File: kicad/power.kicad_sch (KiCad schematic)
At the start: 117 parts, among them J1 12 V in (5.5x2.1), J2 TX power (shunt), U1 TPS54302DDCR, U2 TPS65131RGER, U3 TPS7A4700RGWT, U4 TPS7A3301RGWR, U5 LM2731XMF, U6 TLV75733PDBVR, U7 TPS7A4700RGWT, U8 TPS26600PWPR

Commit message: Board ready for routing: power sheets redrawn, 3D models, test access, routing setup
Schematic
- Power supply split into two boxed A3 sheets (Power 1: input, +5V, VDRV,
  +3V3, 3V3_MIC; Power 2: analog +-6V5, +-5VA, +3V3A and the bring-up notes);
  eFuse wired inline; text no longer clashes; ferrite drawn as L_Ferrite.
- Every page of the schematic PDF is A3 (cells scaled up, array redrawn).
- RX_OUT test pad on every channel; four more GND test points.
- Test pads and solder jumpers out of the BOM, like their footprints.

Board
- 3D model for every part (make_3d.py for the CUSP-TR80, stock substitutes
  for four missing library models); check_design checks it.
- JLC04161H-7628 stackup, ENIG; inner GND layers typed as planes; thermal
  reliefs on through-hole pads; HighCurrent net class (1 mm).
- Custom DRC rules (aesa.kicad_dru): TX/RX and switch-node separation,
  clock spacing, JLCPCB limits.
- Footprints keep their library IDs (schematic parity clean); assembly
  drawing docs/assembly/aesa_assembly.pdf.
- Freerouting 2.5.0 installed; DSN export checked.

ERC 0, DRC 0, design check 19/19, placement checks 12/12.
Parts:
- removed C11, C12, C24, C25, C40, C41: 10u 16V X7R 1206, Capacitor_SMD:C_1206_3216Metric, symbol Device:C
- removed C13: 100n 16V X7R, Capacitor_SMD:C_0603_1608Metric, symbol Device:C
- removed C14: 6.8p 50V C0G, Capacitor_SMD:C_0603_1608Metric, symbol Device:C
- removed C15, C16, C21, C22, C23, C27, C39: 10u 25V X7R 1206, Capacitor_SMD:C_1206_3216Metric, symbol Device:C
- removed C17: 7.5p 50V C0G, Capacitor_SMD:C_0603_1608Metric, symbol Device:C
- removed C18: 220n 16V X7R, Capacitor_SMD:C_0603_1608Metric, symbol Device:C
- removed C19: 10n 16V X7R, Capacitor_SMD:C_0603_1608Metric, symbol Device:C
- removed C20: 4.7n 50V C0G, Capacitor_SMD:C_0603_1608Metric, symbol Device:C
- removed C26, C28, C42: 1u 16V X7R, Capacitor_SMD:C_0603_1608Metric, symbol Device:C
- removed C29: 10n 50V C0G, Capacitor_SMD:C_0603_1608Metric, symbol Device:C
- removed C30: 22u 16V X7R 1210, Capacitor_SMD:C_1210_3225Metric, symbol Device:C
- removed D4, D6: SS14, Diode_SMD:D_SMA, symbol Device:D_Schottky
- removed D5, D7: green, LED_SMD:LED_0603_1608Metric, symbol Device:LED
- removed FB1: 600R@100MHz 0603, Inductor_SMD:L_0603_1608Metric, symbol Device:FerriteBead
- removed JP2, JP3, JP5, JP6, JP7: cut to isolate, Jumper:SolderJumper-2_P1.3mm_Bridged_RoundedPad1.0x1.5mm, symbol Jumper:SolderJumper_2_Bridged
- removed L2, L3: 4.7u Isat>=2A, Inductor_SMD:L_Sunlord_SWPA6045S, symbol Device:L
- removed R10, R13: 3.3k 1%, Resistor_SMD:R_0603_1608Metric, symbol Device:R
- removed R11: 649k 1%, Resistor_SMD:R_0603_1608Metric, symbol Device:R
- removed R12: 121k 1%, Resistor_SMD:R_0603_1608Metric, symbol Device:R
- removed R14: 715k 1%, Resistor_SMD:R_0603_1608Metric, symbol Device:R
- removed R15: 220k 1%, Resistor_SMD:R_0603_1608Metric, symbol Device:R
- removed R7: 100 1%, Resistor_SMD:R_0603_1608Metric, symbol Device:R
- removed R8: 562k 1%, Resistor_SMD:R_0603_1608Metric, symbol Device:R
- removed R9: 130k 1%, Resistor_SMD:R_0603_1608Metric, symbol Device:R
- removed TP12: TP +3V3A, TestPoint:TestPoint_Pad_D1.5mm, symbol Connector:TestPoint
- removed TP3: TP +6V5, TestPoint:TestPoint_Pad_D1.5mm, symbol Connector:TestPoint
- removed TP4: TP -6V5, TestPoint:TestPoint_Pad_D1.5mm, symbol Connector:TestPoint
- removed TP5: TP +5VA, TestPoint:TestPoint_Pad_D1.5mm, symbol Connector:TestPoint
- removed TP6: TP -5VA, TestPoint:TestPoint_Pad_D1.5mm, symbol Connector:TestPoint
- removed U2: TPS65131RGER, Package_DFN_QFN:VQFN-24-1EP_4x4mm_P0.5mm_EP2.45x2.45mm_ThermalVias, symbol Regulator_Switching:TPS65130RGE
- removed U3, U7: TPS7A4700RGWT, Package_DFN_QFN:Texas_RGW0020A_VQFN-20-1EP_5x5mm_P0.65mm_EP3.15x3.15mm_ThermalVias, symbol Regulator_Linear:TPS7A4701xRGW
- removed U4: TPS7A3301RGWR, Package_DFN_QFN:Texas_RGW0020A_VQFN-20-1EP_5x5mm_P0.65mm_EP3.15x3.15mm_ThermalVias, symbol Regulator_Linear:TPS7A3301RGW
- added FB1: 600R@100MHz 0603, Inductor_SMD:L_0603_1608Metric, symbol Device:L_Ferrite
- added TP16, TP17, TP18, TP19: GND, TestPoint:TestPoint_Pad_D1.5mm, symbol Connector:TestPoint
- JP1, JP4: now left out of the parts list
- TP1: value TP VIN -> VIN; now left out of the parts list
- TP10, TP9: value TP GND -> GND; now left out of the parts list
- TP11: value TP 3V3_MIC -> 3V3_MIC; now left out of the parts list
- TP13: value TP VIN_JACK -> VIN_JACK; now left out of the parts list
- TP14: value TP IMON -> IMON; now left out of the parts list
- TP15: value TP FLT -> FLT; now left out of the parts list
- TP2: value TP +5V -> +5V; now left out of the parts list
- TP7: value TP VDRV -> VDRV; now left out of the parts list
- TP8: value TP +3V3 -> +3V3; now left out of the parts list
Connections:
- net +3V3: now also FB1.1
- net 3V3_MIC: now also FB1.2
- net GND: now also TP16.1, TP17.1, TP18.1, TP19.1
- net EF_DVDT: no longer names the net of C43.1, U8.12 (dVdT)
- net EF_FLT: no longer names the net of R27.2, TP15.1, U8.14 (~{FLT})
- net EF_ILIM: no longer names the net of R25.1, U8.11 (ILIM)
- net EF_IMON: no longer names the net of R26.1, TP14.1, U8.10 (IMON)
- net EF_OVP: no longer names the net of R23.2, R24.1, U8.5 (OVP)
- net EF_UVLO: no longer names the net of R22.2, R23.1, U8.3 (UVLO)
- net LED_+3V3: no longer names the net of D10.2 (A), R20.2
- net LED_+5V: no longer names the net of D3.2 (A), R6.2
- net LED_3V3_MIC: no longer names the net of D11.2 (A), R21.2
- net LED_VDRV: no longer names the net of D9.2 (A), R19.2
- net LED_VIN: no longer names the net of D2.2 (A), R1.2
- no-connect marks 19 -> 3
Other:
- note added: "1 A, stable with ceramic caps. Load < 0.15 A: ADC IOVDD, clock buffers, logic, mics."
- note added: "1.23 V x (1 + 150k/13k) = 15.4 V. Load, all 64 elements in CW at 40 kHz: about 0.24 A (sim/reports/tx_cw.md). Remove the"
- note added: "1.6 A. F1 (2 A polyfuse) backs it up."
- note added: "A. 12 V INPUT: jack -> TPS26600 eFuse -> polyfuse -> VIN"
- note added: "E. VDRV 15 V: LM2731X boost from VIN"
- note added: "F. +3V3: TLV75733P LDO from +5V"
- note added: "Ferrite-filtered +3V3 for the 8 MEMS mics. Remove FB1 to isolate."
- note added: "G. GROUND"
- note added: "H. 3V3_MIC: mic supply"
- note added: "J2 shunt to unpower every TX driver."
- note added: "One GND net and plane (In1, In2). Scope-ground test points: TP9/TP10 at the"
- note added: "Power tree and bring-up checklist: Power 2."
- note added: "UVLO/OVP divider 100k / 5.6k / 10k. ILIM 12 k/A -> 7.5k = 1.6 A. dVdT 22 nF: 5 V/ms soft start. IMON 72 uA/A into 15k = 1.08 V/A (TP IMON). FLT"
- note added: "Vout = 0.596 V x (1 + 75k/10k) = 5.07 V. EN UVLO about 7.3 V. Load about 1.6 A. SW_5V loop (C3, U1, L1) kept tight on the board."
- note added: "eFuse U8 (resettable, auto-retry): rated +-60 V (reverse polarity), on above 8.8 V, off above 13.8 V (protects the 14.5 V LM2731), current limit"
- note added: "low = fault (TP FLT). MODE open = auto-retry, SHDN open = on."
- note added: "power supply, TP16-TP19 spread over the board (ADC row, array sides, TX row)."
- note removed: "+5VA: ANY-OUT 1.4 + 3.2 + 0.4 = 5.0 V. -5VA = -1.176 V x (1 + 715k/220k) = -5.00 V."
- note removed: "+6V5 = 1.213 V x (1 + 562k/130k) = 6.46 V. -6V5 = -1.213 V x 649k/121k = -6.51 V."
- note removed: "1.23 V x (1 + 150k/13k) = 15.4 V. Load, all 64 elements in CW at 40 kHz: about 0.24 A (sim/reports/tx_cw.md)."
- note removed: "A. 12 V INPUT: jack -> TPS26600 eFuse (resettable: auto-retry) -> polyfuse (back-up) -> VIN"
- note removed: "ANY-OUT 1.4 + 1.6 + 0.2 + 0.1 = 3.3 V. Load about 0.45 A (16 x TLV320ADC5140); 0.8 W in the LDO, thermal vias under the pad."
- note removed: "C. +-6V5: TPS65131RGER boost + inverter from +5V (feeds the analog LDOs only)"
- note removed: "D. ANALOG RAILS: TPS7A4700 +5VA, TPS7A3301 -5VA (low noise, no LEDs)"
- note removed: "Drawn with the pin-identical TPS65130 symbol: order TPS65131RGER (2 A switches). PSP/PSN low: fixed-frequency PWM."
- note removed: "E. VDRV 15 V: LM2731X boost from VIN. Remove the J2 shunt to unpower all TX drivers"
- note removed: "F. +3V3: TLV75733P LDO from +5V (1 A, stable with ceramic caps)"
- note removed: "G. GROUND: one GND net and plane"
- note removed: "H. 3V3_MIC: ferrite-filtered supply for the 8 MEMS mics (remove FB1 to isolate)"
- note removed: "I. +3V3A: TPS7A4700 low-noise LDO from +5V for the 16 ADCs' AVDD (analog rail: no LED)"
- note removed: "Load < 0.15 A: ADC IOVDD, clock buffers, logic, mics."
- note removed: "Load: 64 x OPA1678 (4 mA per channel): about 0.3 A on +5VA and on -5VA."
- note removed: "Test points for scope grounds."
- note removed: "UVLO/OVP divider 100k / 5.6k / 10k: on 8.8 V, off 13.8 V. ILIM 12 k/A -> 7.5 k = 1.6 A. dVdT 22 nF: 5 V/ms. IMON 72 uA/A into 15 k = 1.08 V/A (TP14). FLT low = fault (TP15)."
- note removed: "Vout = 0.596 V x (1 + 75k/10k) = 5.07 V. EN UVLO about 7.3 V. Load about 1.6 A."
- note removed: "eFuse: input rated 60 V and -60 V (reverse polarity), switches off above 13.8 V (protects the 14.5 V LM2731) and below 8.8 V, current limit 1.6 A."
- title: Power: 12 V in, +5V, +-6V5, +-5VA, VDRV, +3V3, 3V3_MIC, +3V3A -> Power 1: 12 V input, +5V, VDRV (TX), +3V3, 3V3_MIC

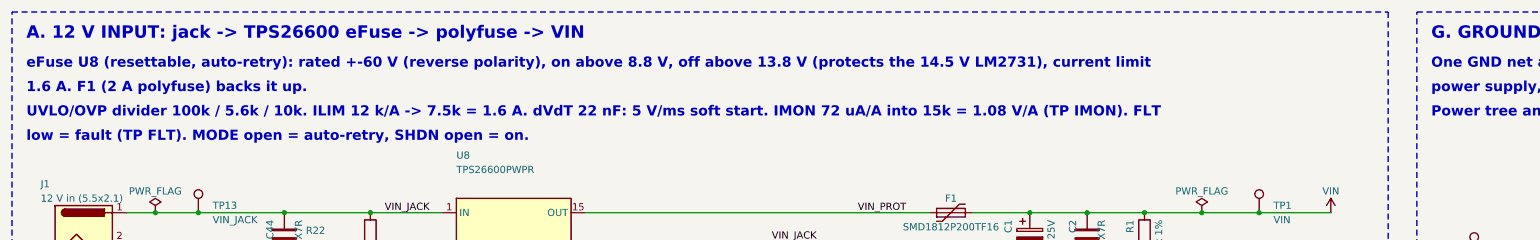
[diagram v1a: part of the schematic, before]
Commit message: Fix small inconsistencies: one revision (rev 1, 2026-10-24) for sheets and board
- REV/DATE come from scripts/common.py for every title block and the board
  silkscreen (the sheets said rev 2, the board rev 1).
- Channel note: +27 dB is element -> amplifier output; the ADC pin sees
  +16.5 dB after the divider.
- Board input text 8.8-13.8 V (eFuse UVLO); LM2731 limit 14 V (14.5 V abs max).
- Brief/README: real board size 192 x 301 mm, CUSP-TR80 footprint and pitch
  note, nominal vs simulated gain, board test-point references, 126 pages.
- SKiDL spec uses L_Ferrite like the sheet; dead AD7606/net-tie entries gone.

ERC 0, DRC 0, design check 19/19, placement checks 12/12.
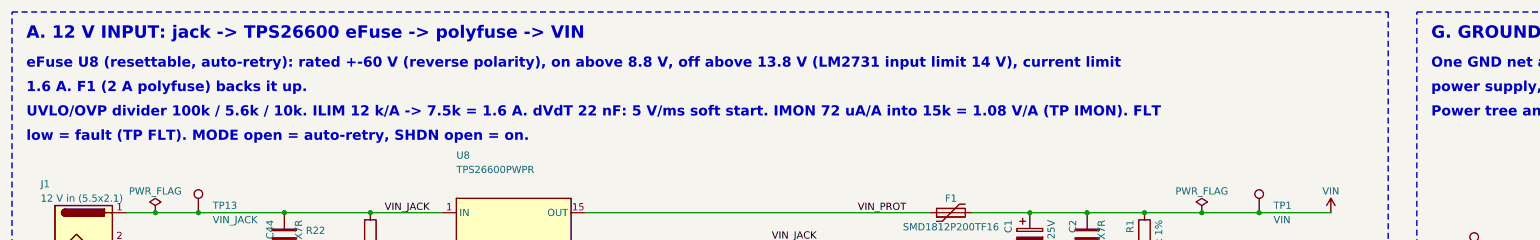
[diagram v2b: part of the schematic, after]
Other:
- note added: "eFuse U8 (resettable, auto-retry): rated +-60 V (reverse polarity), on above 8.8 V, off above 13.8 V (LM2731 input limit 14 V), current limit"
- note removed: "eFuse U8 (resettable, auto-retry): rated +-60 V (reverse polarity), on above 8.8 V, off above 13.8 V (protects the 14.5 V LM2731), current limit"
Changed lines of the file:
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@@
 	(title_block
 		(title "Power 1: 12 V input, +5V, VDRV (TX), +3V3, 3V3_MIC")
-		(date "2026-10-20")
-		(rev "2")
+		(date "2026-10-24")
+		(rev "1")
 		(company "Hybrid 8x8 ultrasonic AESA")
 	)
@@
 		)
 	)
-	(text "eFuse U8 (resettable, auto-retry): rated +-60 V (reverse polarity), on above 8.8 V, off above 13.8 V (protects the 14.5 V LM2731), current limit"
+	(text "eFuse U8 (resettable, auto-retry): rated +-60 V (reverse polarity), on above 8.8 V, off above 13.8 V (LM2731 input limit 14 V), current limit"
 		(exclude_from_sim no)
 		(at 20.32 30.48 0)

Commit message: Block-first routing: all repeated blocks routed and passing, power input and +-6V5 hand-routed
Schematic
- TX groups and ADC inputs numbered in order (TXG01 = DRV1-4, ADC IN1..4 = RX1..4).
- Power sheets renumbered 1-8 with real references; eFuse RTN no longer tied to GND (TPS2660 9.3.5.5).
- Damped 100 uF bulk caps at the far ends of VIN (C50) and +5V (C51); header clock RC filters removed;
  switch-node snubbers kept as DNP footprints.

Layout and routing
- New routing toolchain: route.py (block stages), block_routes.py (hand-made block routes), maze.py
  (45-degree grid router with rip-up and a per-net time budget), route_lib.py (bend45, chamfer, copper
  checks), block_check.py (DRC and internal nets per block instance), board/cell views.
- Channel, ADC, TX group, clock buffer, enable buffer, mic and header blocks routed and passing
  block_check; no right-angle corners left.
- Designed TX control bus; SDI taps keep 0.7 mm from clock copper.
- Power: 12 V input (eFuse, RTN island, FLT via the front copper) and TPS65131 +-6V5 section with fixed
  templates and hand routing; each power section counts as its own block; the +3V3 LED overflows into
  the gap beside its section.

docs/routing_and_emi.md describes the routing and EMI rules; sim/mic_clock_si adds the mic clock check.
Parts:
- added C45: 10u 50V X7R 1210, Capacitor_SMD:C_1210_3225Metric, symbol Device:C
- added C46, C49: 470p 50V C0G DNP, Capacitor_SMD:C_0603_1608Metric, symbol Device:C
- added C50, C51: 100u 25V, Capacitor_SMD:CP_Elec_8x10, symbol Device:C_Polarized
- added L5: 1u Isat>=4A, Inductor_SMD:L_Sunlord_SWPA4030S, symbol Device:L
- added R28, R31: 4.7 1% DNP, Resistor_SMD:R_0603_1608Metric, symbol Device:R
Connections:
- net +5V: now also C51.1
- net GND: now also C45.2, C46.2, C49.2, C50.2, C51.2; no longer C43.2, R24.2, R25.2, R26.2, U8.17 (RTN), U8.8 (RTN)
- net SW_5V: now also R28.1
- net SW_VDRV: now also R31.1
- net VIN: now also C50.1, L5.2; no longer F1.2
- new net: C49.1, R31.2
- new net: C46.1, R28.2
- new net EFUSE_RTN: C43.2, R24.2, R25.2, R26.2, U8.17 (RTN), U8.8 (RTN)
- new net VIN_F: C45.1, F1.2, L5.1
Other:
- note added: "(sim/reports/tx_cw.md). Remove the J9502 shunt to unpower every TX driver. R9531 + C9549: switch-node snubber, DNP (fit"
- note added: "/ TP9510 at the power supply, TP9516 - TP9519 spread over the board (ADC row,"
- note added: "1. 12 V INPUT: jack J9501 -> TPS26600 eFuse U9508 -> polyfuse F9501 -> VIN"
- note added: "1.23 V x (1 + 150k/13k) = 15.4 V (R9517 / R9518). Load, all 64 elements in CW at 40 kHz: about 0.24 A"
- note added: "1.6 A. Polyfuse F9501 (2 A) backs it up. C9545 - L9505 - C9501 keep the switchers' ripple off the cable."
- note added: "2. +5V: TPS54302 buck U9501 (TI reference design), 3 A"
- note added: "3. +3V3: TLV75733P LDO U9506 from +5V"
- note added: "4. VDRV 15 V: LM2731X boost U9505 from VIN"
- note added: "5. 3V3_MIC: mic supply"
- note added: "C9503 - U9501 - L9501 is kept tight on the board. R9528 + C9546: switch-node snubber, DNP (fit only if the switch node rings)."
- note added: "C9551 100 uF electrolytic: damped bulk at the end of the 300 mm +5V run from the buck,"
- note added: "Ferrite-filtered +3V3 for the 8 MEMS mics. Remove FB9501 to isolate."
- note added: "GROUND TEST POINTS"
- note added: "One GND net and plane (inner layers In1, In2). Scope-ground test points: TP9509"
- note added: "RTN (pin 8, PowerPad) and the support parts sit on EFUSE_RTN, apart from GND: the chip's reverse-polarity block is between RTN and GND (tying"
- note added: "UVLO/OVP divider R9522 / R9523 / R9524 (100k / 5.6k / 10k). ILIM R9525 7.5k = 1.6 A. dVdT C9543 22 nF: 5 V/ms soft start. IMON R9526 15k = 1.08"
- note added: "V/A (TP9514). FLT low = fault (TP9515). MODE open = auto-retry, SHDN open = on."
- note added: "Vout = 0.596 V x (1 + 75k/10k) = 5.07 V (R9504 / R9505). EN UVLO about 7.3 V (R9502 / R9503). Load about 1.6 A. The switching loop"
- note added: "both array sides, TX row). Power tree and bring-up checklist: Power 2."
- note added: "current local)."
- note added: "eFuse U9508 (resettable, auto-retry): rated +-60 V (reverse polarity), on above 8.8 V, off above 13.8 V (LM2731 input limit 14 V), current limit"
- note added: "for both top LDOs (U9506, U9507)."
- note added: "mm feed from the jack (its ESR damps the feed inductance against the ceramic input caps; keeps the switchers' ripple"
- note added: "only if the switch node rings). C9550 100 uF electrolytic: damped bulk on VIN at the power row, the far end of the 280"
- note added: "them disables it). Board: an RTN copper island under U9508, clear of the GND planes."
- note removed: "1.23 V x (1 + 150k/13k) = 15.4 V. Load, all 64 elements in CW at 40 kHz: about 0.24 A (sim/reports/tx_cw.md). Remove the"
- note removed: "1.6 A. F1 (2 A polyfuse) backs it up."
- note removed: "A. 12 V INPUT: jack -> TPS26600 eFuse -> polyfuse -> VIN"
- note removed: "B. +5V: TPS54302 buck (TI reference design), 3 A"
- note removed: "E. VDRV 15 V: LM2731X boost from VIN"
- note removed: "F. +3V3: TLV75733P LDO from +5V"
- note removed: "Ferrite-filtered +3V3 for the 8 MEMS mics. Remove FB1 to isolate."
- note removed: "G. GROUND"
- note removed: "H. 3V3_MIC: mic supply"
- note removed: "J2 shunt to unpower every TX driver."
- note removed: "One GND net and plane (In1, In2). Scope-ground test points: TP9/TP10 at the"
- note removed: "Power tree and bring-up checklist: Power 2."
- note removed: "UVLO/OVP divider 100k / 5.6k / 10k. ILIM 12 k/A -> 7.5k = 1.6 A. dVdT 22 nF: 5 V/ms soft start. IMON 72 uA/A into 15k = 1.08 V/A (TP IMON). FLT"
- note removed: "Vout = 0.596 V x (1 + 75k/10k) = 5.07 V. EN UVLO about 7.3 V. Load about 1.6 A. SW_5V loop (C3, U1, L1) kept tight on the board."
- note removed: "eFuse U8 (resettable, auto-retry): rated +-60 V (reverse polarity), on above 8.8 V, off above 13.8 V (LM2731 input limit 14 V), current limit"
- note removed: "low = fault (TP FLT). MODE open = auto-retry, SHDN open = on."
- note removed: "power supply, TP16-TP19 spread over the board (ADC row, array sides, TX row)."
